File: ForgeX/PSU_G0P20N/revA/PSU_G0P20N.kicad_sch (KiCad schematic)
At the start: 48 parts, among them J1 Screw_Terminal_01x02, J2 Conn_02x05_Odd_Even, J4 Conn_01x04, U1 VIPER26LDTR, U2 TL431DBZ, U4 PC817SC_C20612450, U5 MT2492

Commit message: PSUG0_simulation & Doc start
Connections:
- net GND is gone; now on net +12V: C1.2, C10.2, C11.2, C4.2, C9.2, D4.1 (K), D5.1 (K), J2.3 (Pin_3), J2.4 (Pin_4), J2.7 (Pin_7), J2.8 (Pin_8), R16.2, R9.2, U2.3 (A), U3.6 (S1), U5.2 (GND)
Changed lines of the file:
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@@
+	(wire
+		(pts
+			(xy 229.87 38.1) (xy 229.87 39.37)
+		)
+		(stroke
+			(width 0)
+			(type default)
+		)
+	)
+	(wire
+		(pts
+			(xy 143.51 69.85) (xy 138.43 69.85)
+		)
+		(stroke
+			(width 0)
+			(type default)
+		)
+	)
+	(wire
+		(pts
+			(xy 144.78 148.59) (xy 144.78 151.13)
+		)
+		(stroke
+			(width 0)
+			(type default)
+		)
+	)
+	(wire
+		(pts
+			(xy 137.16 138.43) (xy 144.78 138.43)
+		)
+		(stroke
+			(width 0)
+			(type default)
+		)
+	)
+	(wire
+		(pts
+			(xy 161.29 146.05) (xy 161.29 151.13)
+		)
+		(stroke
+			(width 0)
+			(type default)
+		)
+	)
+	(wire
+		(pts
+			(xy 271.78 17.78) (xy 271.78 20.32)
+		)
+		(stroke
+			(width 0)
+			(type default)
+		)
+	)
+	(wire
+		(pts
+			(xy 172.72 85.09) (xy 194.31 85.09)
+		)
+		(stroke
+			(width 0)
+			(type default)
+		)
+	)
+	(wire
+		(pts
+			(xy 82.55 140.97) (xy 96.52 140.97)
+		)
+		(stroke
+			(width 0)
+			(type default)
+		)
+	)
+	(wire
+		(pts
+			(xy 271.78 29.21) (xy 271.78 27.94)
+		)
+		(stroke
+			(width 0)
+			(type default)
+		)
+	)
+	(wire
+		(pts
+			(xy 143.51 58.42) (xy 138.43 58.42)
+		)
+		(stroke
+			(width 0)
+			(type default)
+		)
+	)
+	(wire
+		(pts
+			(xy 104.14 83.82) (xy 104.14 87.63)
+		)
+		(stroke
+			(width 0)
+			(type default)
+		)
+	)
+	(wire
+		(pts
+			(xy 128.27 43.18) (xy 147.32 43.18)
+		)
+		(stroke
+			(width 0)
+			(type default)
+		)
+	)
+	(wire
+		(pts
+			(xy 247.65 24.13) (xy 243.84 24.13)
+		)
+		(stroke
+			(width 0)
+			(type default)
+		)
+	)
+	(wire
+		(pts
+			(xy 30.48 69.85) (xy 62.23 69.85)
+		)
+		(stroke
+			(width 0)
+			(type default)
+		)
+	)
+	(wire
+		(pts
+			(xy 62.23 67.31) (xy 30.48 67.31)
+		)
+		(stroke
+			(width 0)
+			(type default)
+		)
+	)
+	(wire
+		(pts
+			(xy 30.48 82.55) (xy 30.48 90.17)
+		)
+		(stroke
+			(width 0)
+			(type default)
+		)
+	)
+	(wire
+		(pts
+			(xy 144.78 138.43) (xy 151.13 138.43)
+		)
+		(stroke
+			(width 0)
+			(type default)
+		)
+	)
+	(wire
+		(pts
+			(xy 161.29 151.13) (xy 161.29 154.94)
+		)
+		(stroke
+			(width 0)
+			(type default)
+		)
+	)
+	(wire
+		(pts
+			(xy 236.22 60.96) (xy 241.3 60.96)
+		)
+		(stroke
+			(width 0)
+			(type default)
+		)
+	)
 	(wire
 		(pts
@@
 	(wire
 		(pts
-			(xy 229.87 38.1) (xy 229.87 39.37)
-		)
-		(stroke
-			(width 0)
-			(type default)
-		)
-	)
-	(wire
-		(pts
-			(xy 143.51 69.85) (xy 138.43 69.85)
-		)
-		(stroke
-			(width 0)
-			(type default)
-		)
-	)
-	(wire
-		(pts
-			(xy 144.78 148.59) (xy 144.78 151.13)
-		)
-		(stroke
-			(width 0)
-			(type default)
-		)
-	)
-	(wire
-		(pts
-			(xy 137.16 138.43) (xy 144.78 138.43)
-		)
-		(stroke
-			(width 0)
-			(type default)
-		)
-	)
-	(wire
-		(pts
-			(xy 161.29 146.05) (xy 161.29 151.13)
-		)
-		(stroke
-			(width 0)
-			(type default)
-		)
-	)
-	(wire
-		(pts
-			(xy 271.78 17.78) (xy 271.78 20.32)
-		)
-		(stroke
-			(width 0)
-			(type default)
-		)
-	)
-	(wire
-		(pts
-			(xy 172.72 85.09) (xy 194.31 85.09)
-		)
-		(stroke
-			(width 0)
-			(type default)
-		)
-	)
-	(wire
-		(pts
-			(xy 82.55 140.97) (xy 96.52 140.97)
-		)
-		(stroke
-			(width 0)
-			(type default)
-		)
-	)
-	(wire
-		(pts
-			(xy 271.78 29.21) (xy 271.78 27.94)
-		)
-		(stroke
-			(width 0)
-			(type default)
-		)
-	)
-	(wire
-		(pts
-			(xy 143.51 58.42) (xy 138.43 58.42)
-		)
-		(stroke
-			(width 0)
-			(type default)
-		)
-	)
-	(wire
-		(pts
-			(xy 104.14 83.82) (xy 104.14 87.63)
-		)
-		(stroke
-			(width 0)
-			(type default)
-		)
-	)
-	(wire
-		(pts
-			(xy 128.27 43.18) (xy 147.32 43.18)
-		)
-		(stroke
-			(width 0)
-			(type default)
-		)
-	)
-	(wire
-		(pts
-			(xy 247.65 24.13) (xy 243.84 24.13)
-		)
-		(stroke
-			(width 0)
-			(type default)
-		)
-	)
-	(wire
-		(pts
-			(xy 30.48 69.85) (xy 62.23 69.85)
-		)
-		(stroke
-			(width 0)
-			(type default)
-		)
-	)
-	(wire
-		(pts
-			(xy 62.23 67.31) (xy 30.48 67.31)
-		)
-		(stroke
-			(width 0)
-			(type default)
-		)
-	)
-	(wire
-		(pts
-			(xy 30.48 82.55) (xy 30.48 90.17)
-		)
-		(stroke
-			(width 0)
-			(type default)
-		)
-	)
-	(wire
-		(pts
-			(xy 144.78 138.43) (xy 151.13 138.43)
-		)
-		(stroke
-			(width 0)
-			(type default)
-		)
-	)
-	(wire
-		(pts
-			(xy 161.29 151.13) (xy 161.29 154.94)
-		)
-		(stroke
-			(width 0)
-			(type default)
-		)
-	)
-	(wire
-		(pts
-			(xy 236.22 60.96) (xy 241.3 60.96)
-		)
-		(stroke
-			(width 0)
-			(type default)
-		)
-	)
-	(wire
-		(pts
 			(xy 91.44 46.99) (xy 91.44 67.31)
 		)
@@
 		)
 		(stroke
+			(width 0)
+			(type default)
+		)
+	)
+	(wire
+		(pts
+			(xy 157.48 43.18) (xy 172.72 43.18)
+		)
+		(stroke

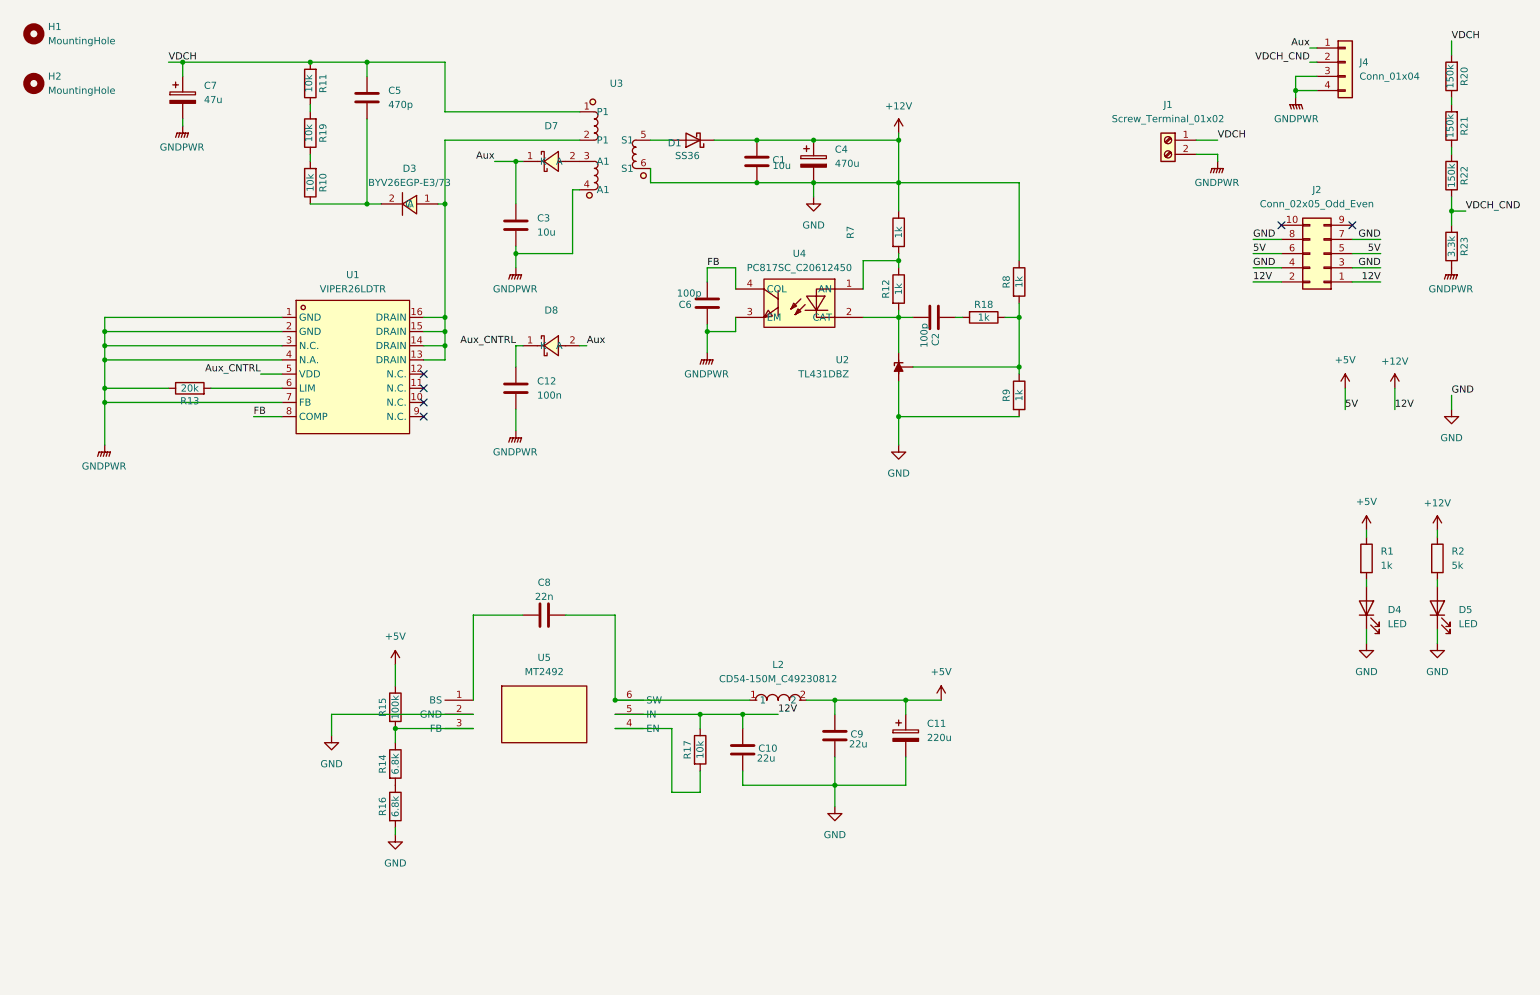
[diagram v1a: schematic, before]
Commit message: PSU Finalization
PSU Documentation semi finalized, sizing, and schematic and layout second pass semi final updates
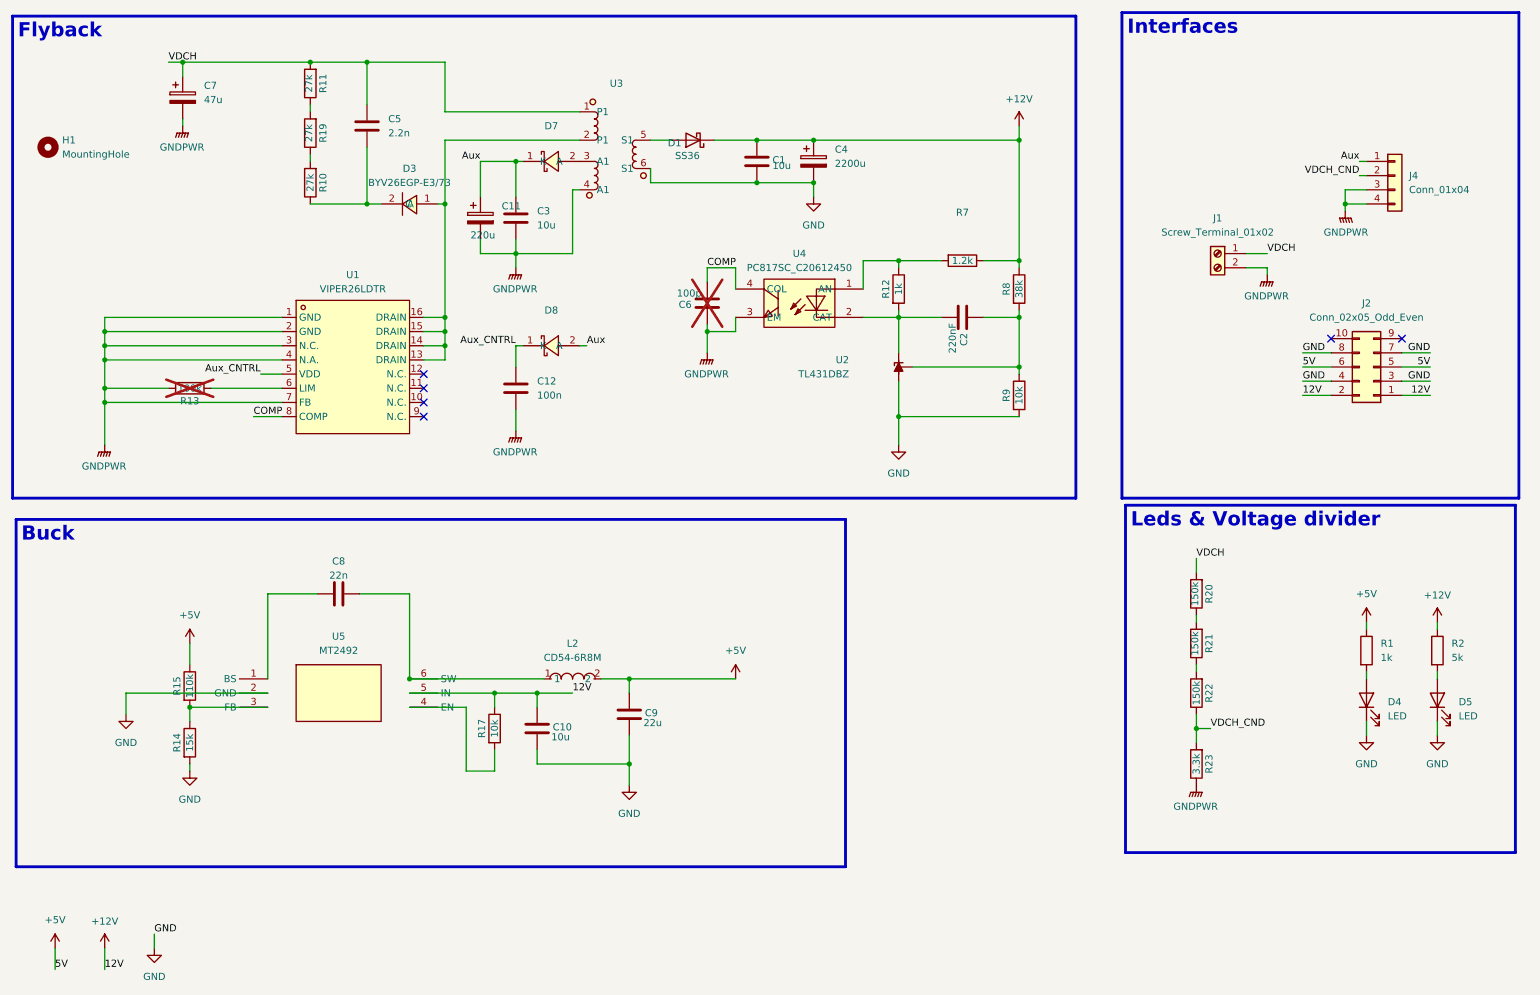
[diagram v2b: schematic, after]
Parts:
- removed H2: MountingHole, MountingHole:MountingHole_2.1mm, symbol Mechanical:MountingHole
- removed R16: 6.8k, Resistor_SMD:R_0603_1608Metric_Pad0.98x0.95mm_HandSolder, symbol Device:R
- removed R18: 1k, Resistor_SMD:R_0603_1608Metric_Pad0.98x0.95mm_HandSolder, symbol Device:R
- C10: value 22u -> 10u
- C11: footprint Capacitor_THT:CP_Radial_D10.0mm_P5.00mm -> Capacitor_THT:CP_Radial_D6.3mm_P2.50mm
- C2: value 100p -> 220nF
- C4: value 470u -> 2200u
- C5: value 470p -> 2.2n
- C6: now not fitted
- L2: value CD54-150M_C49230812 -> CD54-6R8M; LCSC Part C49230812 -> C7588992; MPN CD54-150M -> CD54-6R8M
- R10, R11, R19: value 10k -> 27k
- R13: value 20k -> 100k; now not fitted
- R14: value 6.8k -> 15k
- R15: value 100k -> 110k
- R7: value 1k -> 1.2k
- R8: value 1k -> 38k; Additional Info (none) -> 1%
- R9: value 1k -> 10k
- U3: footprint Libmain:E16 Trans -> Libmain:E22 Trans
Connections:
- net +12V: no longer C1.2, C10.2, C11.2, C4.2, C9.2, D4.1 (K), D5.1 (K), J2.3 (Pin_3), J2.4 (Pin_4), J2.7 (Pin_7), J2.8 (Pin_8), R9.2, U2.3 (A), U3.6 (S1), U5.2 (GND)
- net +5V: no longer C11.1
- net Aux: now also C11.1
- net GNDPWR: now also C11.2
- net at C2.1: now also R8.2, R9.1, U2.2 (REF)
- net GND: now reaches R14.2
- net GND: now also C1.2, C10.2, C4.2, C9.2, D4.1 (K), D5.1 (K), J2.3 (Pin_3), J2.4 (Pin_4), J2.7 (Pin_7), J2.8 (Pin_8), R9.2, U2.3 (A), U3.6 (S1), U5.2 (GND)
- net FB renamed COMP
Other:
- moved on the sheet: C10, C2, C3, C5, C8, C9, D4, D5, H1, J1, J2, J4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
